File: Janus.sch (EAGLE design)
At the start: 16 parts, among them Q1 DMN6140L-7, Q2 DMN6140L-7, U1 SN74LV08APWR, U2 74LVC1G86W5-7, U3 NE555S-13DICT-ND, U4 74HCT1G14GW,125

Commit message: Solved a few issues
Changed Board file to "Janus" to assist with revision control, fixed a
few resistor values and added a printing frame.
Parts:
- R2, R3, R4: value 1M -> 330
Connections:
- net N$5 renamed ONEDIR
- net N$6 renamed CONT_CAP
- new net N$1: Q1.S, Q2.S
- net GND: no longer Q1.S, Q2.S
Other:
- note added: "Board To Board"
- note added: "Board to Cart"
- note added: "Isolation Circuitry"
- note added: "Logic Circuitry"
- note added: "Solenoid Control"
- note added: "Solenoid Delay Circuitry"
- moved on the sheet: C1, C2, D1, Q1, Q2, R1, R2, R3, R4, U1, U2, U3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

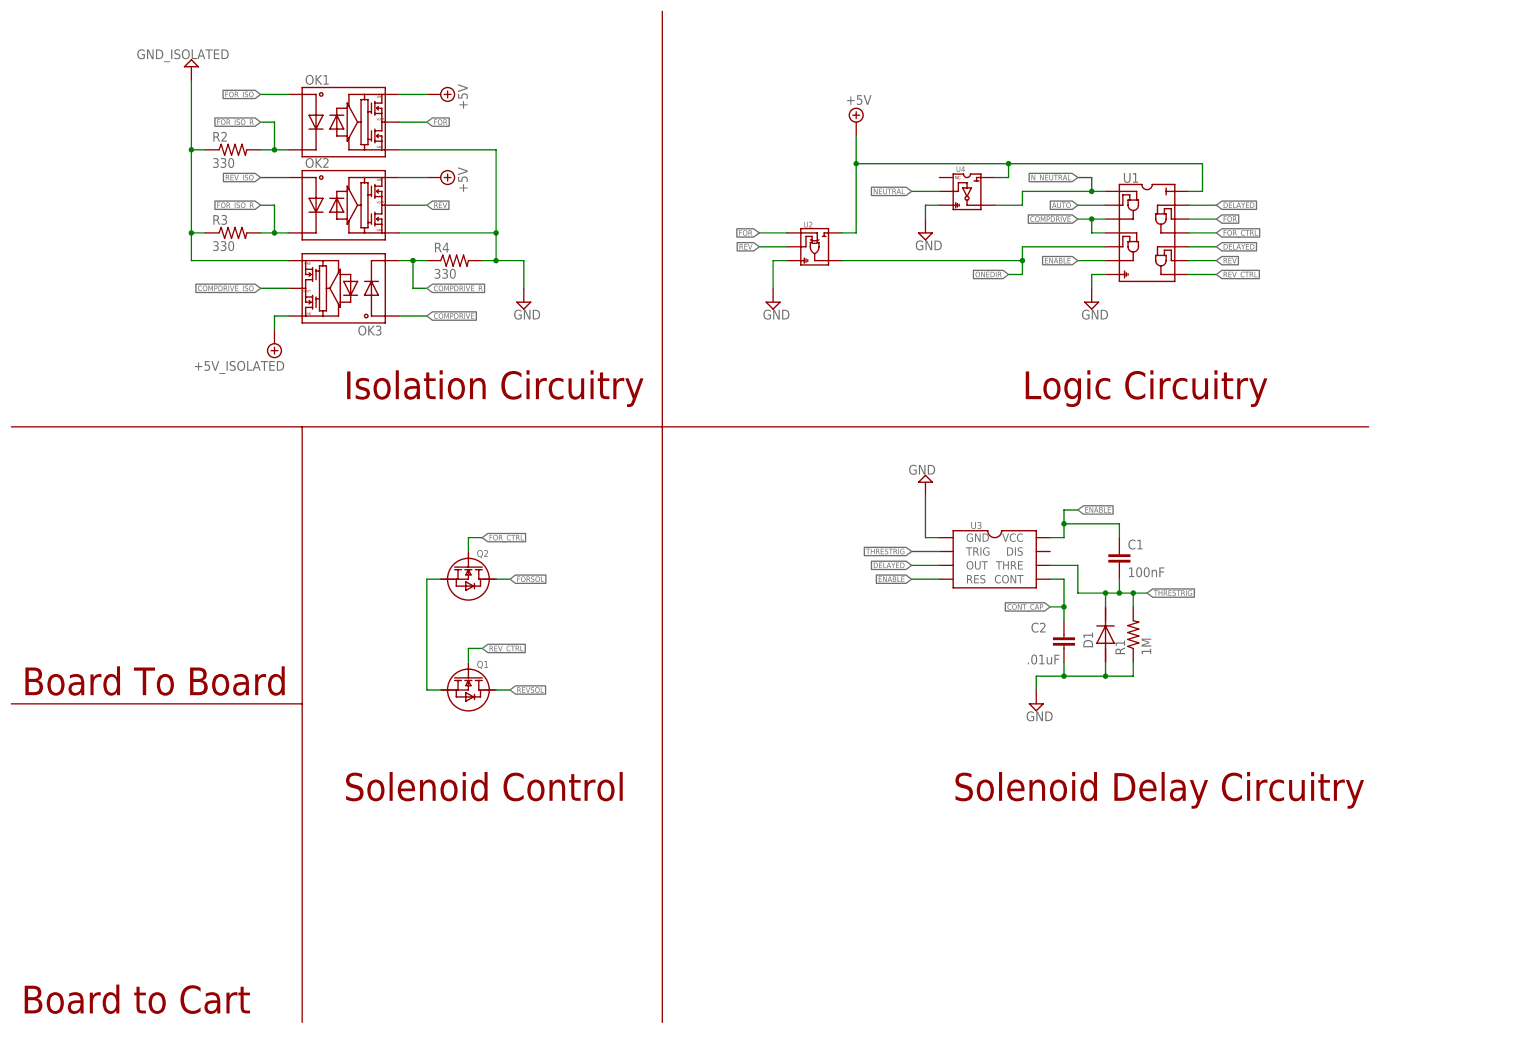
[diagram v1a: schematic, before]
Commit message: Added Parts list
Added parts list to the schematic
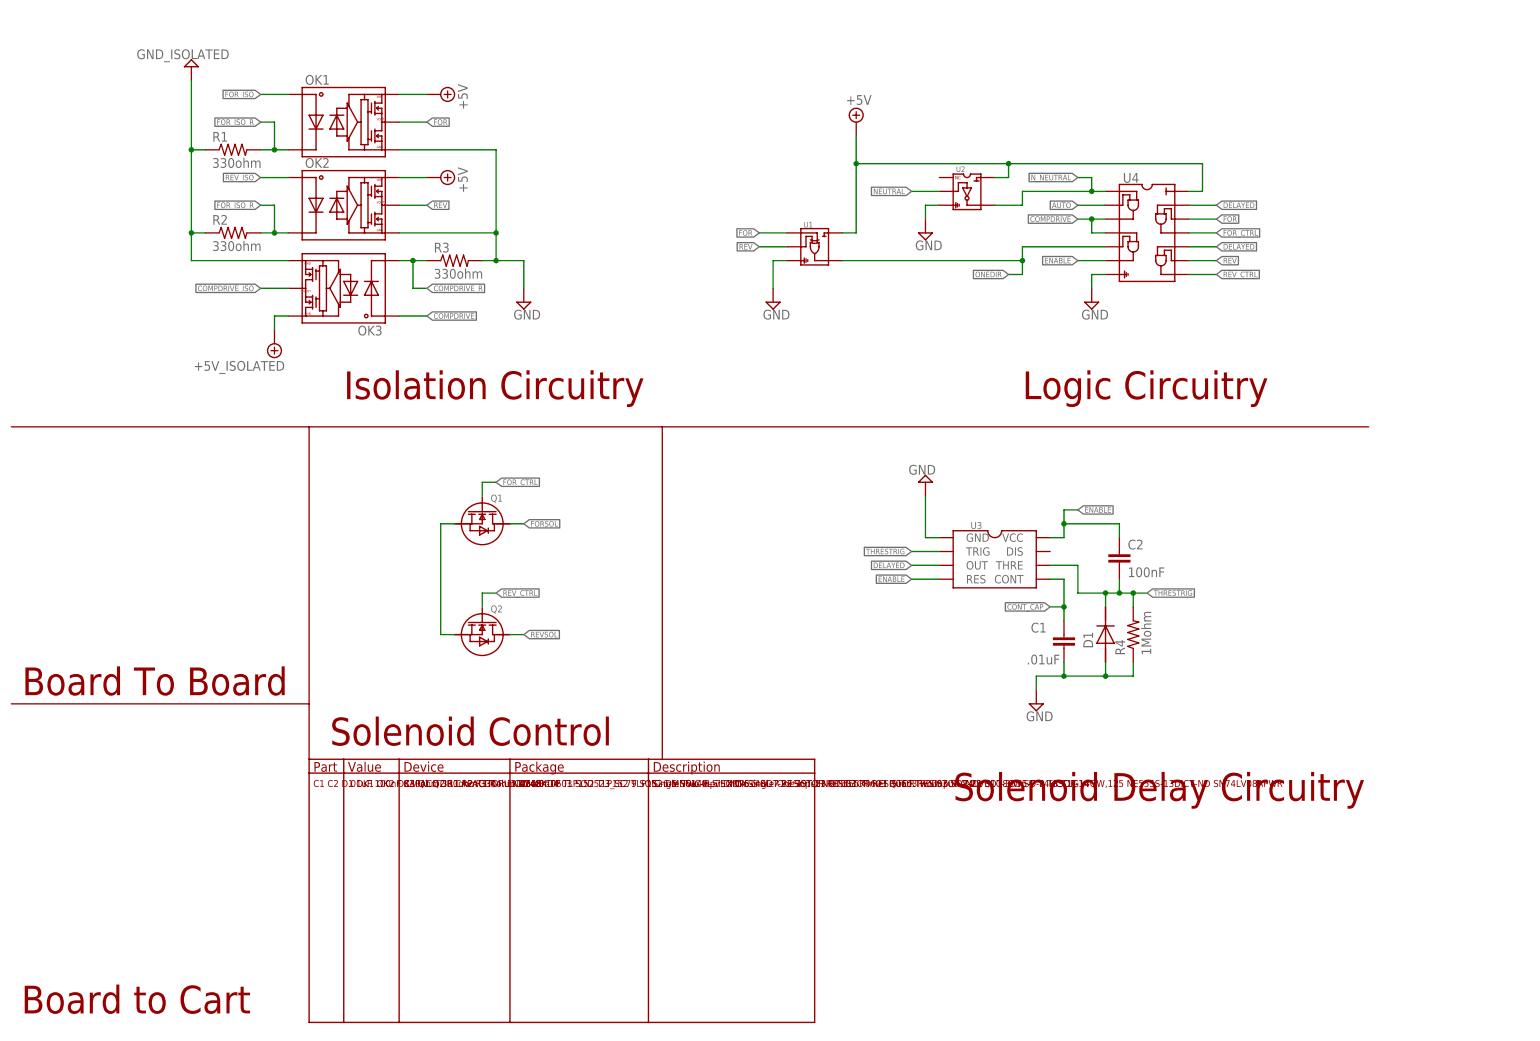
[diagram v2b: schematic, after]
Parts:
- C1: value 100nF -> .01uF
- C2: value .01uF -> 100nF
- R1: value 1M -> 330ohm
- R2, R3: value 330 -> 330ohm
- R4: value 330 -> 1Mohm
- U1: value SN74LV08APWR -> 74LVC1G86W5-7; device CP-IC:SN74LV08APWR -> CP-IC:74LVC1G86W5-7
- U2: value 74LVC1G86W5-7 -> 74HCT1G14GW,125; device CP-IC:74LVC1G86W5-7 -> CP-IC:74HCT1G14GW,125
- U4: value 74HCT1G14GW,125 -> SN74LV08APWR; device CP-IC:74HCT1G14GW,125 -> CP-IC:SN74LV08APWR
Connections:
- net +5V: now also U1.P$5, U4.P$14; no longer U1.P$14, U4.P$5
- net AUTO: now also U4.P$2; no longer U1.P$2
- net COMPDRIVE: now also U4.P$3, U4.P$4; no longer U1.P$3, U1.P$4
- net COMPDRIVE_R: now also R3.1; no longer R4.1
- net CONT_CAP: now also C1.1; no longer C2.1
- net DELAYED: now also U4.P$10, U4.P$13; no longer U1.P$10, U1.P$13
- net ENABLE: now also C2.1, U4.P$6; no longer C1.1, U1.P$6
- net FOR: now also U1.P$1, U4.P$12; no longer U1.P$12, U2.P$1
- net FORSOL: now also Q1.D; no longer Q2.D
- net FOR_CTRL: now also Q1.G, U4.P$11; no longer Q2.G, U1.P$11
- net FOR_ISO_R: now also R1.2; no longer R3.2
- net GND: now also C1.2, R3.2, R4.1, U1.P$3, U4.P$7; no longer C2.2, R3.1, R4.2, U1.P$7, U4.P$3
- net NEUTRAL: now also U2.P$2; no longer U4.P$2
- net N_NEUTRAL: now also U2.P$4, U4.P$1; no longer U1.P$1, U4.P$4
- net ONEDIR: now also U1.P$4, U4.P$5; no longer U1.P$5, U2.P$4
- net REV: now also U1.P$2, U4.P$9; no longer U1.P$9, U2.P$2
- net REVSOL: now also Q2.D; no longer Q1.D
- net REV_CTRL: now also Q2.G, U4.P$8; no longer Q1.G, U1.P$8
- net THRESTRIG: now also C2.2, R4.2; no longer C1.2, R1.2
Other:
- moved on the sheet: C1, C2, Q1, Q2, R1, R2, R3, R4
